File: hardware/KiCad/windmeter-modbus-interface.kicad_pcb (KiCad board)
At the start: 2 copper layers, 29 parts, among them J1 MODBUS-P1, J2 Programming, J3 MODBUS-P2, J4 RJ14, J5 RJ14, U1 CH32V003J4M6, U2 MAX3485

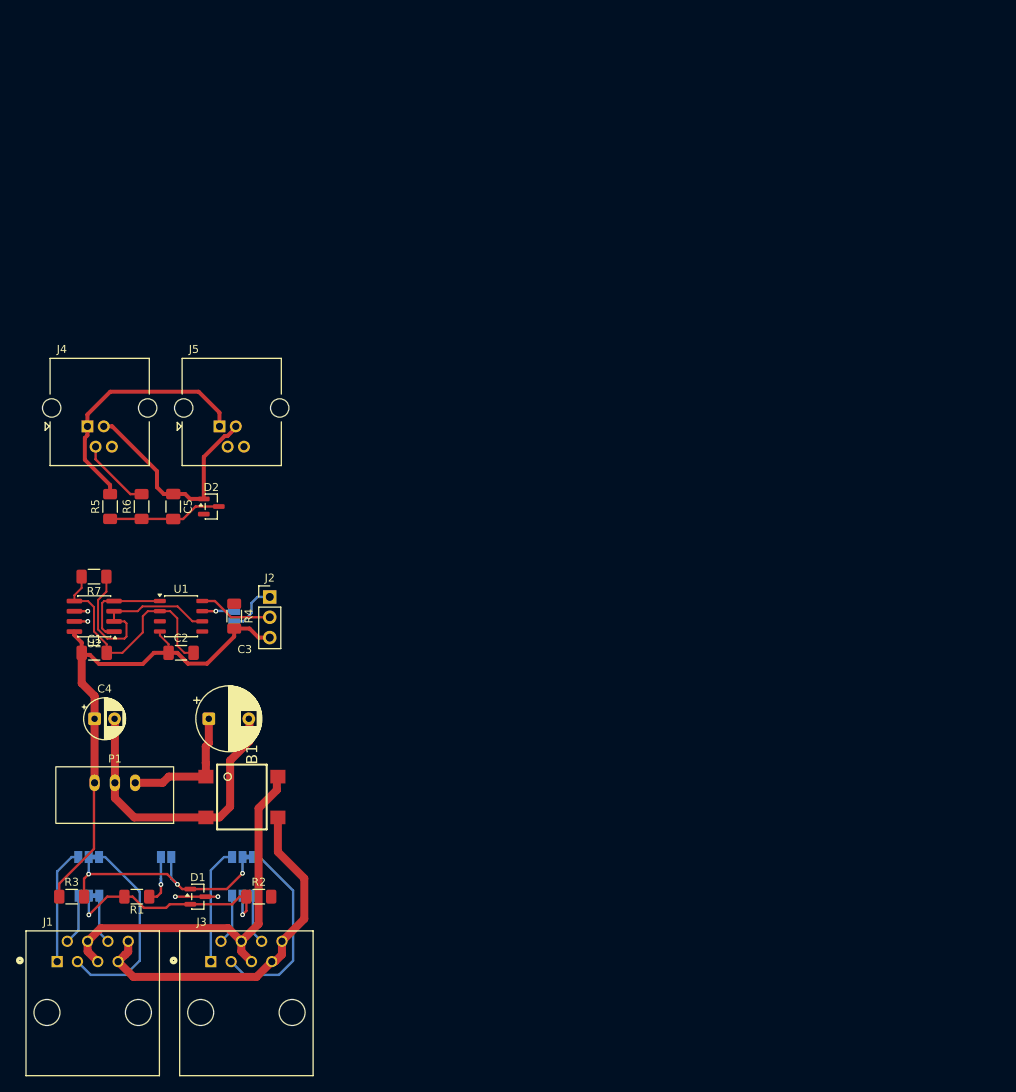
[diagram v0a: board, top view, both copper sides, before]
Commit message: Repository documentation: README, changelog, contributing, licenses
Root docs adapted from the tester-repo templates to this project:
- README: device overview, variant/address table, project status with
  pointers into the design chain, hardware summary, register-map summary,
  repo layout, build/flash/test instructions (incl. acceptance suite and
  submodule clone), related repositories
- changelog: project history to date under [Unreleased] (design chain,
  TDS v0.6, drivers with HIL results, firmware stages A-F, HIL harness);
  release tagging deferred to RELEASES.md's fw-v<N> process
- contributing: correct repo URL, requirements-first workflow (TDS IDs),
  build/test expectations, *_test binaries never released
- LICENSE/license.md: project name corrected; third-party section names
  the actual manufacturers and covers the KiCad library submodules

Co-Authored-By: Claude Fable 5 <noreply@anthropic.com>
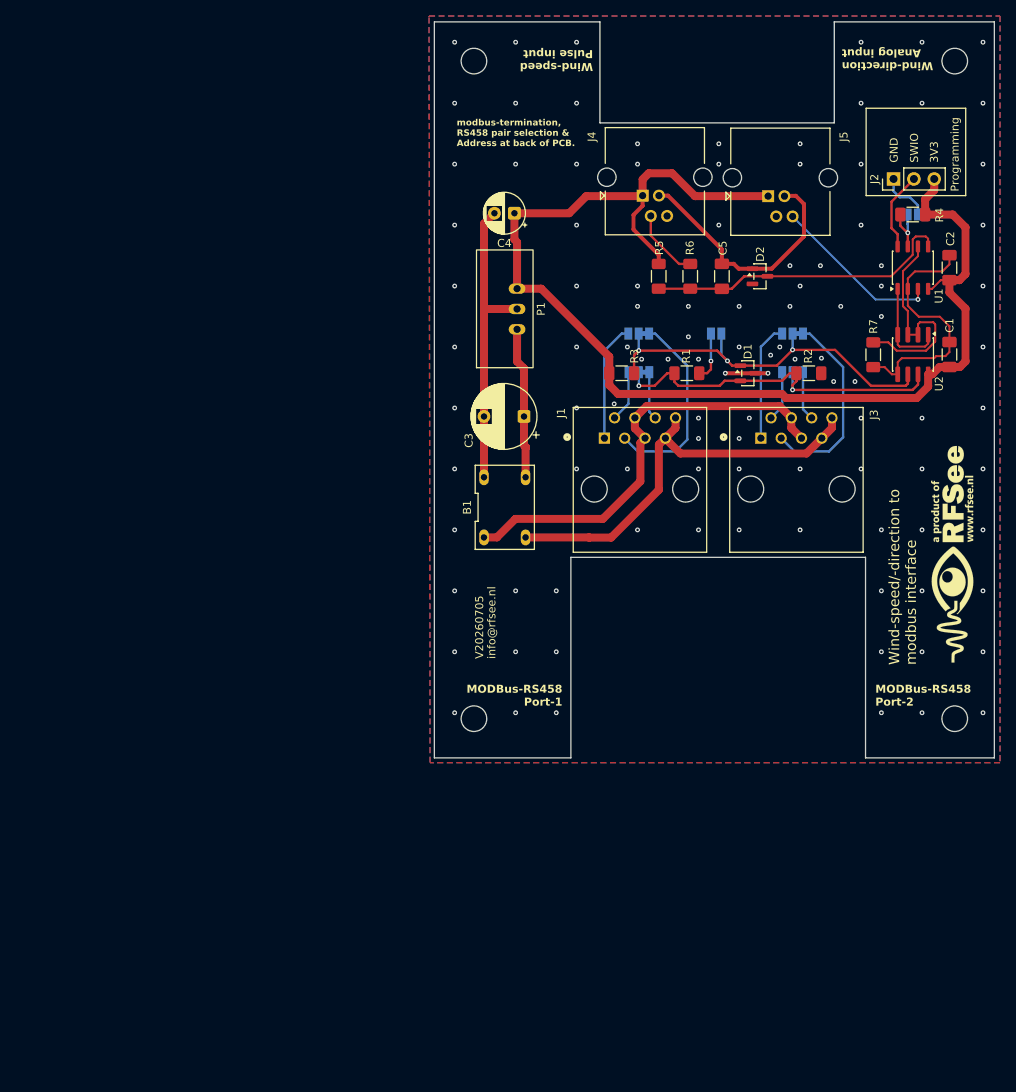
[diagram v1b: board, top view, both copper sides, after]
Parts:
- added G***: LOGO_LogoRFSee_28x5-6mm, my-KiCad-library:LOGO_LogoRFSee_28x5-6mm, F.Cu at (217.2, 114.8)
- B1: footprint my-KiCad-library:DB207 -> my-KiCad-library:DB207-DIP-4
- moved C1 113.2 mm to (216.8, 89.8), turned to 90 degrees
- moved U2 107.4 mm to (212.2, 89.8), turned to -90 degrees
- moved C2 107.4 mm to (216.8, 79.0), turned to 90 degrees
- moved U1 101.3 mm to (212.2, 79.0), turned to 90 degrees
- moved R7 101.3 mm to (207.3, 89.9), turned to -90 degrees
- moved JP6 98.6 mm to (212.2, 72.3), turned to 180 degrees
- moved R4 98.6 mm to (212.2, 72.3), turned to 0 degrees
- moved J3 94.9 mm to (197.7, 106.7)
- moved D1 94.9 mm to (191.6, 92.2)
- moved JP1 94.9 mm to (187.6, 87.2)
- moved JP3 94.9 mm to (177.9, 87.2)
- moved JP4 94.9 mm to (197.2, 92.1)
- moved JP5 94.9 mm to (197.2, 87.2)
- moved R1 94.9 mm to (184.0, 92.2)
- moved R3 94.9 mm to (175.8, 92.2)
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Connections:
- B1 pad -: Net-(P1-GND) -> /GND
- C3 pad 2: Net-(P1-GND) -> /GND
- C4 pad 2: Net-(P1-GND) -> /GND
- P1 pad 2: Net-(P1-GND) -> /GND
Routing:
- net /3V3: track 99.1 -> 155.4 mm
- net /GND: track 71.1 -> 113.0 mm, vias 2 -> 105
- net Net-(P1-GND): track 37.9 -> 0.00 mm
- net /PULSE_IN: track 14.2 -> 38.6 mm
- net /ANALOG_IN: track 0.00 -> 21.4 mm, vias 0 -> 1
- net /RS485-B: track 30.9 -> 45.8 mm, vias 3 -> 2
- net /RS485-A: track 34.6 -> 49.5 mm, vias 4 -> 3
- net /-24V: track 45.3 -> 53.2 mm
- net /+24V: track 49.2 -> 55.0 mm
- net /ADDRESS: track 4.00 -> 6.71 mm
- net Net-(P1-IN): track 16.5 -> 19.0 mm
- net Net-(JP1-A): track 6.90 -> 6.13 mm
- net /SWIO: track 9.28 -> 9.91 mm
- added copper zone on B.Cu, net /GND
- added copper zone on F.Cu, net /GND
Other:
- board outline added: 70 x 92 mm
- board text added: "3V3"
- board text added: "A"
- board text added: "Address select"
- board text added: "B"
- board text added: "Enable termination"
- board text added: "GND"
- board text added: "MB1"
- board text added: "MB2"
- board text added: "MODBus-RS458 Port-1"
- board text added: "MODBus-RS458 Port-2"
- board text added: "Pair selector 1"
- board text added: "Pair selector 2"
- board text added: "Programming"
- board text added: "SWIO"
- board text added: "V20260705"
- board text added: "Wind-direction Analog input"
- board text added: "Wind-speed Pulse input"
- board text added: "Wind-speed/-direction to modbus interface"
- board text added: "https://github.com/pe1mew/windmeters-modbus-interface"
- board text added: "info@rfsee.nl"
- board text added: "modbus-termination, RS458 pair selection & Address at back of PCB."
